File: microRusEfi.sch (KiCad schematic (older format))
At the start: 13 parts, among them U3 Molex_48_pin

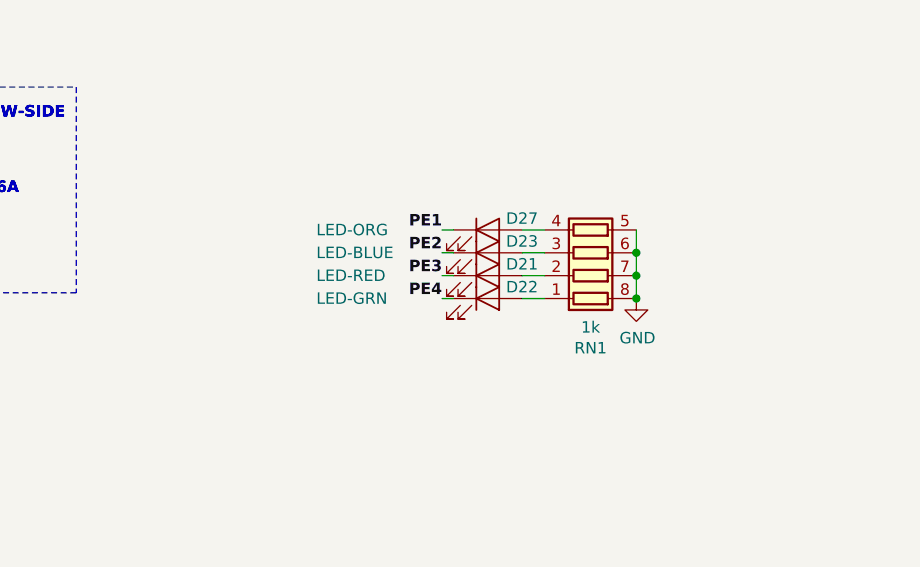
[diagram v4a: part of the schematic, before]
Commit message: Added LED note to schematic and PCB silk. https://github.com/rusefi/hw_microRusEfi/issues/57
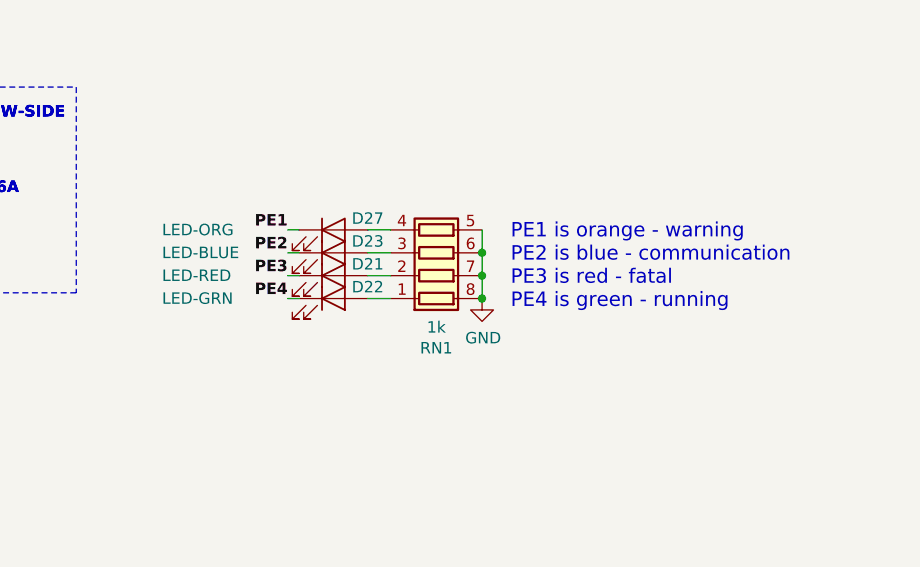
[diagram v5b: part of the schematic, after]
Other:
- note added: "PE1 is orange - warning\nPE2 is blue - communication\nPE3 is red - fatal\nPE4 is green - running"
- moved on the sheet: D21, D22, D23, D27, RN1
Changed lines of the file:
@@
 Text Label 6700 8525 2    50   ~ 10
 PE4
-Text Label 14350 5850 2    50   ~ 10
+Text Label 13675 5850 2    50   ~ 10
 PE1
 $Comp
 L Device:LED D22
 U 1 1 5E7651E5
-P 14550 6150
-F 0 "D22" H 14700 6200 50  0000 C CNN
-F 1 "LED-GRN" H 13800 6150 50  0000 L CNN
-F 2 "LED_SMD:LED_0603_1608Metric" H 14550 6150 50  0001 C CNN
-F 3 "~" H 14550 6150 50  0001 C CNN
-F 4 "LTST-C191KGKT" H -100 0   50  0001 C CNN "Part #"
-F 5 "DIGI" H -100 0   50  0001 C CNN "VEND"
-F 6 "160-1446-1-ND" H -100 0   50  0001 C CNN "VEND#"
-F 7 "Lite-On " H -100 0   50  0001 C CNN "Manufacturer"
-	1    14550 6150
+P 13875 6150
+F 0 "D22" H 14025 6200 50  0000 C CNN
+F 1 "LED-GRN" H 13125 6150 50  0000 L CNN
+F 2 "LED_SMD:LED_0603_1608Metric" H 13875 6150 50  0001 C CNN
+F 3 "~" H 13875 6150 50  0001 C CNN
+F 4 "LTST-C191KGKT" H -775 0   50  0001 C CNN "Part #"
+F 5 "DIGI" H -775 0   50  0001 C CNN "VEND"
+F 6 "160-1446-1-ND" H -775 0   50  0001 C CNN "VEND#"
+F 7 "Lite-On " H -775 0   50  0001 C CNN "Manufacturer"
+	1    13875 6150
 	1    0    0    -1
 $EndComp
@@
 L Device:LED D21
 U 1 1 5D1B59E8
-P 14550 6050
-F 0 "D21" H 14700 6100 50  0000 C CNN
-F 1 "LED-RED" H 13800 6050 50  0000 L CNN
-F 2 "LED_SMD:LED_0603_1608Metric" H 14550 6050 50  0001 C CNN
-F 3 "~" H 14550 6050 50  0001 C CNN
-F 4 "LTST-S270KRKT" H -100 0   50  0001 C CNN "Part #"
-F 5 "DIGI" H -100 0   50  0001 C CNN "VEND"
-F 6 "160-1479-1-ND" H -100 0   50  0001 C CNN "VEND#"
-F 7 "Lite-On " H -100 0   50  0001 C CNN "Manufacturer"
-	1    14550 6050
+P 13875 6050
+F 0 "D21" H 14025 6100 50  0000 C CNN
+F 1 "LED-RED" H 13125 6050 50  0000 L CNN
+F 2 "LED_SMD:LED_0603_1608Metric" H 13875 6050 50  0001 C CNN
+F 3 "~" H 13875 6050 50  0001 C CNN
+F 4 "LTST-S270KRKT" H -775 0   50  0001 C CNN "Part #"
+F 5 "DIGI" H -775 0   50  0001 C CNN "VEND"
+F 6 "160-1479-1-ND" H -775 0   50  0001 C CNN "VEND#"
+F 7 "Lite-On " H -775 0   50  0001 C CNN "Manufacturer"
+	1    13875 6050
 	1    0    0    -1
 $EndComp
@@
 L Device:LED D23
 U 1 1 5D1BAEB2
-P 14550 5950
-F 0 "D23" H 14700 6000 50  0000 C CNN
-F 1 "LED-BLUE" H 13800 5950 50  0000 L CNN
-F 2 "LED_SMD:LED_0603_1608Metric" H 14550 5950 50  0001 C CNN
-F 3 "~" H 14550 5950 50  0001 C CNN
-F 4 "LTST-C193TBKT-5A" H -100 0   50  0001 C CNN "Part #"
-F 5 "DIGI" H -100 0   50  0001 C CNN "VEND"
-F 6 "160-1827-1-ND" H -100 0   50  0001 C CNN "VEND#"
-F 7 "Lite-On " H -100 0   50  0001 C CNN "Manufacturer"
-	1    14550 5950
+P 13875 5950
+F 0 "D23" H 14025 6000 50  0000 C CNN
+F 1 "LED-BLUE" H 13125 5950 50  0000 L CNN
+F 2 "LED_SMD:LED_0603_1608Metric" H 13875 5950 50  0001 C CNN
+F 3 "~" H 13875 5950 50  0001 C CNN
+F 4 "LTST-C193TBKT-5A" H -775 0   50  0001 C CNN "Part #"
+F 5 "DIGI" H -775 0   50  0001 C CNN "VEND"
+F 6 "160-1827-1-ND" H -775 0   50  0001 C CNN "VEND#"
+F 7 "Lite-On " H -775 0   50  0001 C CNN "Manufacturer"
+	1    13875 5950
 	1    0    0    -1
 $EndComp
@@
 L Device:LED D27
 U 1 1 5D1C01C9
-P 14550 5850
-F 0 "D27" H 14700 5900 50  0000 C CNN
-F 1 "LED-ORG" H 13800 5850 50  0000 L CNN
-F 2 "LED_SMD:LED_0603_1608Metric" H 14550 5850 50  0001 C CNN
-F 3 "~" H 14550 5850 50  0001 C CNN
-F 4 "LTST-C190KFKT" H -100 0   50  0001 C CNN "Part #"
-F 5 "DIGI" H -100 0   50  0001 C CNN "VEND"
-F 6 "160-1434-1-ND" H -100 0   50  0001 C CNN "VEND#"
-F 7 "Lite-On " H -100 0   50  0001 C CNN "Manufacturer"
-	1    14550 5850
-	1    0    0    -1
-$EndComp
-Text Label 14350 5950 2    50   ~ 10
+P 13875 5850
+F 0 "D27" H 14025 5900 50  0000 C CNN
+F 1 "LED-ORG" H 13125 5850 50  0000 L CNN
+F 2 "LED_SMD:LED_0603_1608Metric" H 13875 5850 50  0001 C CNN
+F 3 "~" H 13875 5850 50  0001 C CNN
+F 4 "LTST-C190KFKT" H -775 0   50  0001 C CNN "Part #"
+F 5 "DIGI" H -775 0   50  0001 C CNN "VEND"
+F 6 "160-1434-1-ND" H -775 0   50  0001 C CNN "VEND#"
+F 7 "Lite-On " H -775 0   50  0001 C CNN "Manufacturer"
+	1    13875 5850
+	1    0    0    -1
+$EndComp
+Text Label 13675 5950 2    50   ~ 10
 PE2
-Text Label 14350 6050 2    50   ~ 10
+Text Label 13675 6050 2    50   ~ 10
 PE3
-Text Label 14350 6150 2    50   ~ 10
+Text Label 13675 6150 2    50   ~ 10
 PE4
 $Comp
 L Device:R_Pack04 RN1
 U 1 1 5CF9A0A2
-P 15000 5950
-F 0 "RN1" V 14583 5950 50  0000 C CNN
-F 1 "1k" V 14674 5950 50  0000 C CNN
-F 2 "Resistor_SMD:R_Array_Convex_4x0603" V 15275 5950 50  0001 C CNN
-F 3 "~" H 15000 5950 50  0001 C CNN
-F 4 "EXB-V8V102JV" H 0   0   50  0001 C CNN "Part #"
-F 5 "DIGI" H 0   0   50  0001 C CNN "VEND"
-F 6 "Y4102CT-ND" H 0   0   50  0001 C CNN "VEND#"
-F 7 "Panasonic " H 0   0   50  0001 C CNN "Manufacturer"
-	1    15000 5950
+P 14325 5950
+F 0 "RN1" V 13908 5950 50  0000 C CNN
+F 1 "1k" V 13999 5950 50  0000 C CNN
+F 2 "Resistor_SMD:R_Array_Convex_4x0603" V 14600 5950 50  0001 C CNN
+F 3 "~" H 14325 5950 50  0001 C CNN
+F 4 "EXB-V8V102JV" H -675 0   50  0001 C CNN "Part #"
+F 5 "DIGI" H -675 0   50  0001 C CNN "VEND"
+F 6 "Y4102CT-ND" H -675 0   50  0001 C CNN "VEND#"
+F 7 "Panasonic " H -675 0   50  0001 C CNN "Manufacturer"
+	1    14325 5950
 	0    1    -1   0
 $EndComp
@@
 L power:GND #PWR0214
 U 1 1 5CFDDBE0
-P 15200 6150
-F 0 "#PWR0214" H 15200 5900 50  0001 C CNN
-F 1 "GND" H 15205 5977 50  0000 C CNN
-F 2 "" H 15200 6150 50  0001 C CNN
-F 3 "" H 15200 6150 50  0001 C CNN
-	1    15200 6150
-	1    0    0    -1
-$EndComp
-Wire Wire Line
-	15200 5850 15200 5950
-Connection ~ 15200 6150
-Connection ~ 15200 5950
-Wire Wire Line
-	15200 5950 15200 6050
-Connection ~ 15200 6050
-Wire Wire Line
-	15200 6050 15200 6150
+P 14525 6150
+F 0 "#PWR0214" H 14525 5900 50  0001 C CNN
+F 1 "GND" H 14530 5977 50  0000 C CNN
+F 2 "" H 14525 6150 50  0001 C CNN
+F 3 "" H 14525 6150 50  0001 C CNN
+	1    14525 6150
+	1    0    0    -1
+$EndComp
+Wire Wire Line
+	14525 5850 14525 5950
+Connection ~ 14525 6150
+Connection ~ 14525 5950
+Wire Wire Line
+	14525 5950 14525 6050
+Connection ~ 14525 6050
+Wire Wire Line
+	14525 6050 14525 6150
 NoConn ~ 7950 8000
 NoConn ~ 7950 8100
@@
 $EndComp
 Wire Wire Line
-	14700 5850 14800 5850
-Wire Wire Line
-	14700 5950 14800 5950
-Wire Wire Line
-	14700 6050 14800 6050
-Wire Wire Line
-	14700 6150 14800 6150
+	14025 5850 14125 5850
+Wire Wire Line
+	14025 5950 14125 5950
+Wire Wire Line
+	14025 6050 14125 6050
+Wire Wire Line
+	14025 6150 14125 6150
 Connection ~ 8500 3400
 Wire Wire Line
@@
 CAN BE USED AS LOW-SIDE \nOR HIGH-SIDE
 Wire Wire Line
-	14350 5850 14400 5850
-Wire Wire Line
-	14350 5950 14400 5950
-Wire Wire Line
-	14350 6050 14400 6050
-Wire Wire Line
-	14350 6150 14400 6150
+	13675 5850 13725 5850
+Wire Wire Line
+	13675 5950 13725 5950
+Wire Wire Line
+	13675 6050 13725 6050
+Wire Wire Line
+	13675 6150 13725 6150
+Text Notes 14650 6200 0    63   ~ 0
+PE1 is orange - warning\nPE2 is blue - communication\nPE3 is red - fatal\nPE4 is green - running
 $EndSCHEMATC

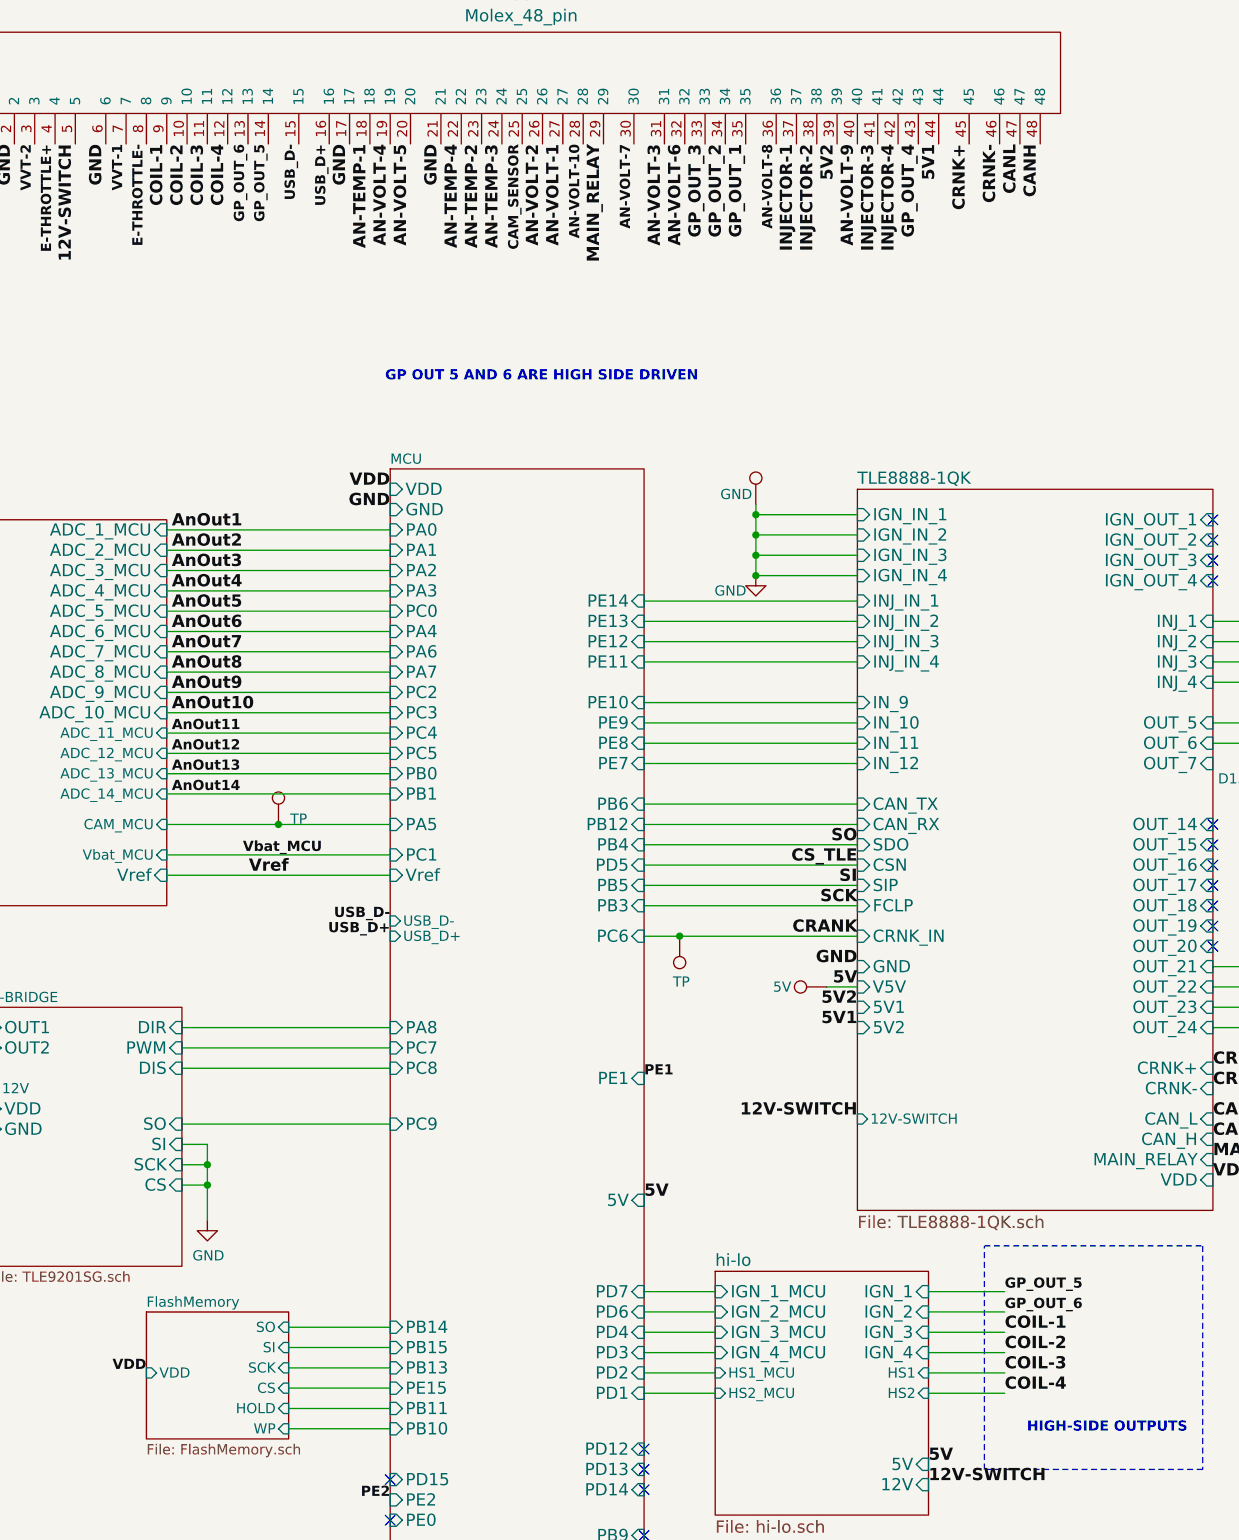
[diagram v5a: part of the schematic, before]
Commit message: Changed net names, per issue 63, also added many thermal via's and several electrical GND via's. https://github.com/rusefi/hw_microRusEfi/issues/63
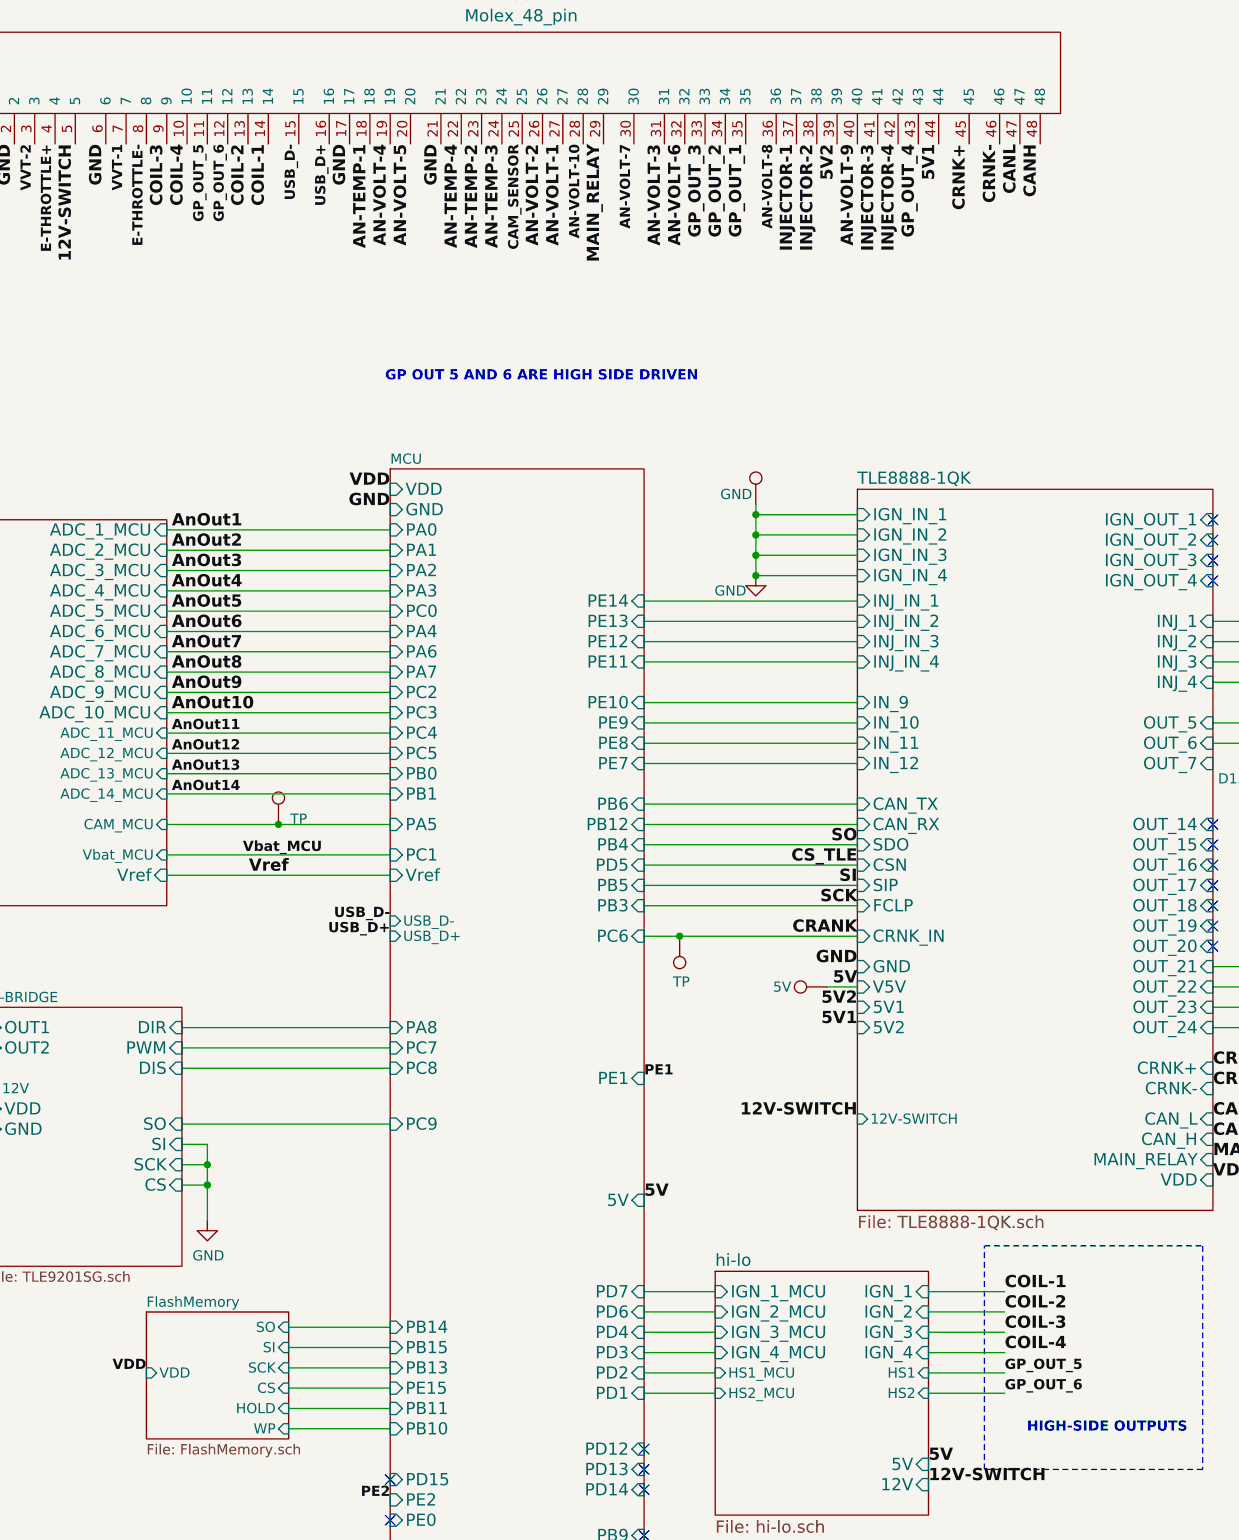
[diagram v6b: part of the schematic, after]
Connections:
- net COIL-1: now also U3.14; no longer U3.9
- net COIL-2: now also U3.13; no longer U3.10
- net COIL-3: now also U3.9; no longer U3.11
- net COIL-4: now also U3.10; no longer U3.12
- net GP_OUT_5: now also U3.11; no longer U3.14
- net GP_OUT_6: now also U3.12; no longer U3.13
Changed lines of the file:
@@
 Text Label 6200 5175 2    60   ~ 12
 Vref
-Text Label 9725 7625 0    60   ~ 12
-COIL-3
-Text Label 9725 7425 0    60   ~ 12
-COIL-1
-Text Label 9725 7525 0    60   ~ 12
-COIL-2
-Text Label 9725 7725 0    60   ~ 12
-COIL-4
 Text Label 11675 4025 0    60   ~ 12
 INJECTOR-2
@@
 Text Label 9800 1575 3    60   ~ 12
 CANL
-Text Label 5900 1575 3    60   ~ 12
+Text Label 5700 1575 3    60   ~ 12
 COIL-4
-Text Label 5700 1575 3    60   ~ 12
-COIL-2
-Text Label 5600 1575 3    60   ~ 12
-COIL-1
-Text Label 5800 1575 3    60   ~ 12
-COIL-3
 Text Label 4750 1575 3    60   ~ 12
 12V-SWITCH
@@
 	1    0    0    -1
 $EndComp
-Text Label 6000 1575 3    50   ~ 10
-GP_OUT_6
 Text Label 7750 1575 3    60   ~ 12
 MAIN_RELAY
@@
 Wire Wire Line
 	10750 5925 11725 5925
-Text Label 6100 1575 3    50   ~ 10
-GP_OUT_5
-Text Label 9725 7325 0    50   ~ 10
-GP_OUT_6
-Text Label 9725 7225 0    50   ~ 10
-GP_OUT_5
 Wire Notes Line
 	11575 3550 11575 4800
@@
 Text Notes 14650 6200 0    63   ~ 0
 PE1 is orange - warning\nPE2 is blue - communication\nPE3 is red - fatal\nPE4 is green - running
+Text Label 9725 7525 0    60   ~ 12
+COIL-4
+Text Label 5600 1575 3    60   ~ 12
+COIL-3
+Text Label 9725 7425 0    60   ~ 12
+COIL-3
+Text Label 6000 1575 3    60   ~ 12
+COIL-2
+Text Label 9725 7325 0    60   ~ 12
+COIL-2
+Text Label 9725 7725 0    50   ~ 10
+GP_OUT_6
+Text Label 5900 1575 3    50   ~ 10
+GP_OUT_6
+Text Label 9725 7625 0    50   ~ 10
+GP_OUT_5
+Text Label 9725 7225 0    60   ~ 12
+COIL-1
+Text Label 6100 1575 3    60   ~ 12
+COIL-1
+Text Label 5800 1575 3    50   ~ 10
+GP_OUT_5
 $EndSCHEMATC

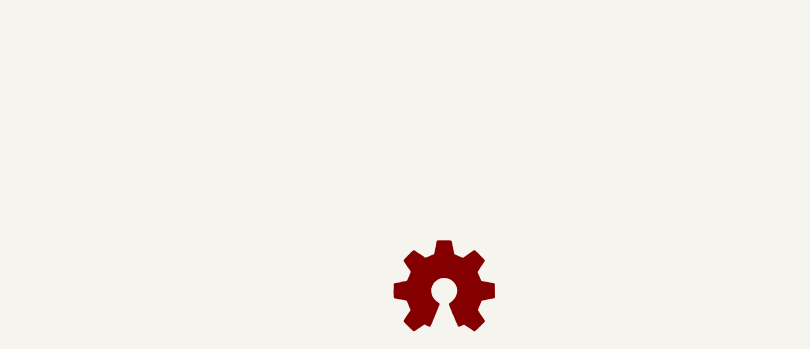
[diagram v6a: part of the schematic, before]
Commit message: Added branding per issue 68, as well added 1,2,3,4 copper layer to clarify to PCB MFG's what the stack up is. https://github.com/rusefi/hw_microRusEfi/issues/68
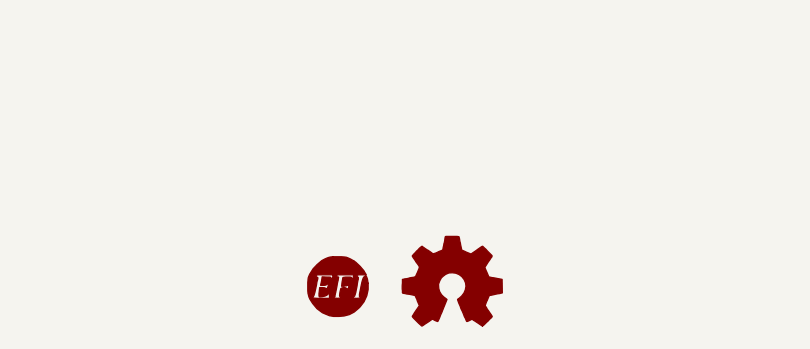
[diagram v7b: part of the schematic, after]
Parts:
- added LOGO2: DNP, rusEFI:LOGO, symbol rusefi_Logo:LOGO
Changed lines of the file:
@@
 L Graphic:Logo_Open_Hardware_Small LOGO1
 U 1 1 5D21BC70
-P 11890 10245
-F 0 "LOGO1" H 11890 10520 50  0001 C CNN
-F 1 "DNP" H 11890 10020 50  0001 C CNN
-F 2 "modules:Logo" H 11890 10245 50  0001 C CNN
-F 3 "~" H 11890 10245 50  0001 C CNN
-F 4 "DNP" H 0   0   50  0001 C CNN "Part #"
-F 5 "DNP" H 0   0   50  0001 C CNN "VEND"
-F 6 "DNP" H 0   0   50  0001 C CNN "VEND#"
-F 7 "DNP" H 0   0   50  0001 C CNN "Manufacturer"
-	1    11890 10245
+P 11925 10225
+F 0 "LOGO1" H 11925 10500 50  0001 C CNN
+F 1 "DNP" H 11925 10000 50  0001 C CNN
+F 2 "modules:Logo" H 11925 10225 50  0001 C CNN
+F 3 "~" H 11925 10225 50  0001 C CNN
+F 4 "DNP" H 35  -20 50  0001 C CNN "Part #"
+F 5 "DNP" H 35  -20 50  0001 C CNN "VEND"
+F 6 "DNP" H 35  -20 50  0001 C CNN "VEND#"
+F 7 "DNP" H 35  -20 50  0001 C CNN "Manufacturer"
+	1    11925 10225
 	1    0    0    -1
 $EndComp
@@
 Text Label 5800 1575 3    50   ~ 10
 GP_OUT_5
+$Comp
+L rusefi_Logo:LOGO LOGO2
+U 1 1 5D54AA23
+P 11425 10225
+F 0 "LOGO2" H 11425 10500 50  0001 C CNN
+F 1 "DNP" H 11425 10000 50  0001 C CNN
+F 2 "rusEFI:LOGO" H 11425 10225 50  0001 C CNN
+F 3 "~" H 11425 10225 50  0001 C CNN
+F 4 "DNP" H -465 -20 50  0001 C CNN "Part #"
+F 5 "DNP" H -465 -20 50  0001 C CNN "VEND"
+F 6 "DNP" H -465 -20 50  0001 C CNN "VEND#"
+F 7 "DNP" H -465 -20 50  0001 C CNN "Manufacturer"
+	1    11425 10225
+	1    0    0    -1
+$EndComp
 $EndSCHEMATC
